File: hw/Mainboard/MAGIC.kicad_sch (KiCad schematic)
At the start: 22 parts, among them SW1 NMI, SW2 RESET, SW4 RESET, U13 Raspberry Pi Zero, U18 SN74LVC4245APWR, U19 SN74LVC4245APWR, U20 SN74LVC4245APWR

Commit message: hw: wip add MCU, 2 layer board
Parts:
- removed C21: 100n, Capacitor_SMD:C_0402_1005Metric, symbol Device:C_Small
- removed SW2: RESET, Button_Switch_THT:SW_Tactile_SPST_Angled_PTS645Vx39-2LFS, symbol Switch:SW_Push
- removed U13: Raspberry Pi Zero, PET:Raspberry Pi Zero W 2, symbol PET:Raspberry Pi Zero W
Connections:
- net A3: now also U19.17 (B5); no longer U19.18 (B4)
- net BA3: now also U19.7 (A5); no longer U19.6 (A4)
- net BHORIZ: now also U20.3 (A1); no longer U20.8 (A6)
- net BR~{W}: now also U20.8 (A6); no longer U19.8 (A6)
- net BVERT: now also U20.4 (A2); no longer U20.9 (A7)
- net B~{PIA1_CS}: now also U20.7 (A5); no longer U20.5 (A3)
- net B~{PIA2_CS}: now also U20.10 (A8); no longer U20.6 (A4)
- net B~{RES}: now also U19.6 (A4); no longer U19.7 (A5)
- net B~{VIA_CS}: now also U20.9 (A7); no longer U20.4 (A2)
- net Bϕ2: now also U20.6 (A4); no longer U20.3 (A1)
- net GND: now also U19.16 (B6); no longer U20.17 (B5)
- net HORIZ: now also U20.21 (B1); no longer U20.16 (B6)
- net R~{W}: now also U20.16 (B6); no longer U19.16 (B6)
- net VERT: now also U20.20 (B2); no longer U20.15 (B7)
- net ~{BVIDEO}: now also U20.5 (A3); no longer U20.10 (A8)
- net ~{PIA1_CS}: now also U20.17 (B5); no longer U20.19 (B3)
- net ~{PIA2_CS}: now also U20.14 (B8); no longer U20.18 (B4)
- net ~{RES}: now also U19.18 (B4); no longer U19.17 (B5)
- net ~{VIA_CS}: now also U20.15 (B7); no longer U20.20 (B2)
- net ~{VIDEO}: now also U20.19 (B3); no longer U20.14 (B8)
- net ϕ2: now also U20.18 (B4); no longer U20.21 (B1)
- no-connect marks 5 -> 3
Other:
- added sheet MCU (MCU.kicad_sch)
- note added: "Shift 5V -> 3.3V: VOUT = VIN * (R2 / (R1 + R2) VIN = 5.1V R1 = 5.6k - 1% R2 = 10k + 1% VOUT = 3.29V"
- note removed: "GPIO2/3 have built-in 1k8 pull ups"
- moved on the sheet: C24, C25, SW1, SW4

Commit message: hw: T8 (wip)
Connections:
- net BHORIZ: now also U20.5 (A3); no longer U20.3 (A1)
- net HORIZ: now also U20.19 (B3); no longer U20.21 (B1)
- net ~{BVIDEO}: now also U20.3 (A1); no longer U20.5 (A3)
- net ~{VIDEO}: now also U20.21 (B1); no longer U20.19 (B3)
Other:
- sheet CPLD ports: added ~{ML}, ~{SO}, ~{VP}; removed A[0..16], D[0..7], PI_A[0..15], PI_CLK, PI_D[0..7], PI_R~{W}, RAM_A[10..11], ~{PI_DONE}, ~{PI_PENDING}
- moved on the sheet: R52, R54, R55, R57, R58, R60

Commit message: hw: routing (excluding MCU)
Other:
- sheet CPLD renamed FPGA
- sheet FPGA ports: added A[0..16], D[0..7], MCU_CLK, RAM_A[10..11], SPI0_RX, SPI0_SCK, SPI0_TX, SPI0_~{CS}, SPI1_RX, SPI1_SCK, SPI1_TX, SPI1_~{CS}, SPI1_~{READY}, ~{CRESET}; removed none
- sheet MCU ports: added MCU_CLK, SPI0_SCK, SPI1_SCK, ~{CRESET}; removed MCU_SPI1_SCLK, SPI0_SCLK
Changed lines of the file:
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@@
+    (stroke (width 0) (type default) (color 0 0 0 0))
+  )
+  (wire (pts (xy 102.87 44.45) (xy 109.22 44.45))
     (stroke (width 0) (type default) (color 0 0 0 0))
   )
@@
     (stroke (width 0) (type default) (color 0 0 0 0))
   )
+  (wire (pts (xy 102.87 68.58) (xy 109.22 68.58))
+    (stroke (width 0) (type default) (color 0 0 0 0))
+  )
   (wire (pts (xy 261.62 144.78) (xy 265.43 144.78))
     (stroke (width 0) (type default) (color 0 0 0 0))
@@
     (stroke (width 0) (type default) (color 0 0 0 0))
   )
+  (wire (pts (xy 102.87 71.12) (xy 109.22 71.12))
+    (stroke (width 0) (type default) (color 0 0 0 0))
+  )
+  (wire (pts (xy 102.87 58.42) (xy 109.22 58.42))
+    (stroke (width 0) (type default) (color 0 0 0 0))
+  )
   (wire (pts (xy 232.41 52.07) (xy 233.68 52.07))
     (stroke (width 0) (type default) (color 0 0 0 0))
@@
     (stroke (width 0) (type default) (color 0 0 0 0))
   )
+  (wire (pts (xy 102.87 39.37) (xy 109.22 39.37))
+    (stroke (width 0) (type default) (color 0 0 0 0))
+  )
   (wire (pts (xy 247.65 76.2) (xy 245.11 76.2))
     (stroke (width 0) (type default) (color 0 0 0 0))
@@
     (stroke (width 0) (type default) (color 0 0 0 0))
   )
+  (wire (pts (xy 102.87 60.96) (xy 109.22 60.96))
+    (stroke (width 0) (type default) (color 0 0 0 0))
+  )
   (wire (pts (xy 262.89 129.54) (xy 261.62 129.54))
     (stroke (width 0) (type default) (color 0 0 0 0))
   )
+  (wire (pts (xy 102.87 55.88) (xy 109.22 55.88))
+    (stroke (width 0) (type default) (color 0 0 0 0))
+  )
   (wire (pts (xy 33.02 139.7) (xy 44.45 139.7))
     (stroke (width 0) (type default) (color 0 0 0 0))
@@
     (stroke (width 0) (type default) (color 0 0 0 0))
   )
+  (wire (pts (xy 102.87 53.34) (xy 109.22 53.34))
+    (stroke (width 0) (type default) (color 0 0 0 0))
+  )
   (wire (pts (xy 149.86 133.35) (xy 149.86 140.97))
     (stroke (width 0) (type default) (color 0 0 0 0))
   )
+  (wire (pts (xy 102.87 41.91) (xy 109.22 41.91))
+    (stroke (width 0) (type default) (color 0 0 0 0))
+  )
   (wire (pts (xy 232.41 46.99) (xy 232.41 49.53))
     (stroke (width 0) (type default) (color 0 0 0 0))
@@
     (stroke (width 0) (type default) (color 0 0 0 0))
   )
+  (wire (pts (xy 102.87 63.5) (xy 109.22 63.5))
+    (stroke (width 0) (type default) (color 0 0 0 0))
+  )
   (wire (pts (xy 204.47 46.99) (xy 208.28 46.99))
     (stroke (width 0) (type default) (color 0 0 0 0))
@@
   )
   (bus (pts (xy 201.93 41.91) (xy 201.93 44.45))
+    (stroke (width 0) (type default) (color 0 0 0 0))
+  )
+  (wire (pts (xy 102.87 46.99) (xy 109.22 46.99))
     (stroke (width 0) (type default) (color 0 0 0 0))
   )
@@
     (stroke (width 0) (type solid) (color 0 0 0 0))
     (fill (color 0 0 0 0.0000))
-    (property "Sheet name" "CPLD" (id 0) (at 109.22 33.5784 0)
+    (property "Sheet name" "FPGA" (id 0) (at 109.22 33.5784 0)
       (effects (font (size 1.27 1.27)) (justify left bottom))
     )
@@
       (effects (font (size 1.27 1.27)) (justify right))
     )
-  )
-  (sheet (at 31.75 27.94) (size 38.1 50.8) (fields_autoplaced)
+    (pin "D[0..7]" bidirectional (at 139.7 44.45 0)
+      (effects (font (size 1.27 1.27)) (justify right))
+    )
+    (pin "RAM_A[10..11]" output (at 139.7 39.37 0)
+      (effects (font (size 1.27 1.27)) (justify right))
+    )
+    (pin "A[0..16]" bidirectional (at 139.7 41.91 0)
+      (effects (font (size 1.27 1.27)) (justify right))
+    )
+    (pin "SPI0_RX" output (at 109.22 44.45 180)
+      (effects (font (size 1.27 1.27)) (justify left))
+    )
+    (pin "SPI0_TX" input (at 109.22 46.99 180)
+      (effects (font (size 1.27 1.27)) (justify left))
+    )
+    (pin "SPI0_~{CS}" input (at 109.22 39.37 180)
+      (effects (font (size 1.27 1.27)) (justify left))
+    )
+    (pin "SPI1_RX" output (at 109.22 58.42 180)
+      (effects (font (size 1.27 1.27)) (justify left))
+    )
+    (pin "SPI1_~{CS}" input (at 109.22 53.34 180)
+      (effects (font (size 1.27 1.27)) (justify left))
+    )
+    (pin "SPI1_TX" input (at 109.22 60.96 180)
+      (effects (font (size 1.27 1.27)) (justify left))
+    )
+    (pin "MCU_CLK" input (at 109.22 68.58 180)
+      (effects (font (size 1.27 1.27)) (justify left))
+    )
+    (pin "SPI0_SCK" input (at 109.22 41.91 180)
+      (effects (font (size 1.27 1.27)) (justify left))
+    )
+    (pin "SPI1_~{READY}" output (at 109.22 63.5 180)
+      (effects (font (size 1.27 1.27)) (justify left))
+    )
+    (pin "SPI1_SCK" input (at 109.22 55.88 180)
+      (effects (font (size 1.27 1.27)) (justify left))
+    )
+    (pin "~{CRESET}" input (at 109.22 71.12 180)
+      (effects (font (size 1.27 1.27)) (justify left))
+    )
+  )
+  (sheet (at 64.77 34.29) (size 38.1 50.8) (fields_autoplaced)
     (stroke (width 0.1524) (type solid) (color 0 0 0 0))
     (fill (color 0 0 0 0.0000))
-    (property "Sheet name" "MCU" (id 0) (at 31.75 27.2284 0)
+    (property "Sheet name" "MCU" (id 0) (at 64.77 33.5784 0)
       (effects (font (size 1.27 1.27)) (justify left bottom))
     )
-    (property "Sheet file" "MCU.kicad_sch" (id 1) (at 31.75 79.3246 0)
+    (property "Sheet file" "MCU.kicad_sch" (id 1) (at 64.77 85.6746 0)
       (effects (font (size 1.27 1.27)) (justify left top))
     )
-    (pin "SPI0_SCLK" output (at 69.85 35.56 0)
-      (effects (font (size 1.27 1.27)) (justify right))
-    )
-    (pin "SPI0_~{CS}" output (at 69.85 33.02 0)
-      (effects (font (size 1.27 1.27)) (justify right))
-    )
-    (pin "SPI0_RX" input (at 69.85 38.1 0)
-      (effects (font (size 1.27 1.27)) (justify right))
-    )
-    (pin "SPI0_TX" output (at 69.85 40.64 0)
-      (effects (font (size 1.27 1.27)) (justify right))
-    )
-    (pin "MCU_SPI1_SCLK" output (at 69.85 48.26 0)
-      (effects (font (size 1.27 1.27)) (justify right))
-    )
-    (pin "SPI1_~{CS}" output (at 69.85 45.72 0)
-      (effects (font (size 1.27 1.27)) (justify right))
-    )
-    (pin "SPI1_RX" input (at 69.85 50.8 0)
-      (effects (font (size 1.27 1.27)) (justify right))
-    )
-    (pin "SPI1_TX" output (at 69.85 53.34 0)
-      (effects (font (size 1.27 1.27)) (justify right))
-    )
-    (pin "SPI1_~{READY}" input (at 69.85 55.88 0)
-      (effects (font (size 1.27 1.27)) (justify right))
-    )
+    (pin "SPI0_~{CS}" output (at 102.87 39.37 0)
+      (effects (font (size 1.27 1.27)) (justify right))
+    )
+    (pin "SPI0_RX" input (at 102.87 44.45 0)
+      (effects (font (size 1.27 1.27)) (justify right))
+    )
+    (pin "SPI0_TX" output (at 102.87 46.99 0)
+      (effects (font (size 1.27 1.27)) (justify right))
+    )
+    (pin "SPI1_~{CS}" output (at 102.87 53.34 0)
+      (effects (font (size 1.27 1.27)) (justify right))
+    )
+    (pin "SPI1_RX" input (at 102.87 58.42 0)
+      (effects (font (size 1.27 1.27)) (justify right))
+    )
+    (pin "SPI1_TX" output (at 102.87 60.96 0)
+      (effects (font (size 1.27 1.27)) (justify right))
+    )
+    (pin "SPI1_~{READY}" input (at 102.87 63.5 0)
+      (effects (font (size 1.27 1.27)) (justify right))
+    )
+    (pin "SPI1_SCK" output (at 102.87 55.88 0)
+      (effects (font (size 1.27 1.27)) (justify right))
+    )
+    (pin "MCU_CLK" output (at 102.87 68.58 0)
+      (effects (font (size 1.27 1.27)) (justify right))
+    )
+    (pin "SPI0_SCK" output (at 102.87 41.91 0)
+      (effects (font (size 1.27 1.27)) (justify right))
+    )
+    (pin "~{CRESET}" output (at 102.87 71.12 0)
+      (effects (font (size 1.27 1.27)) (justify right))
+    )

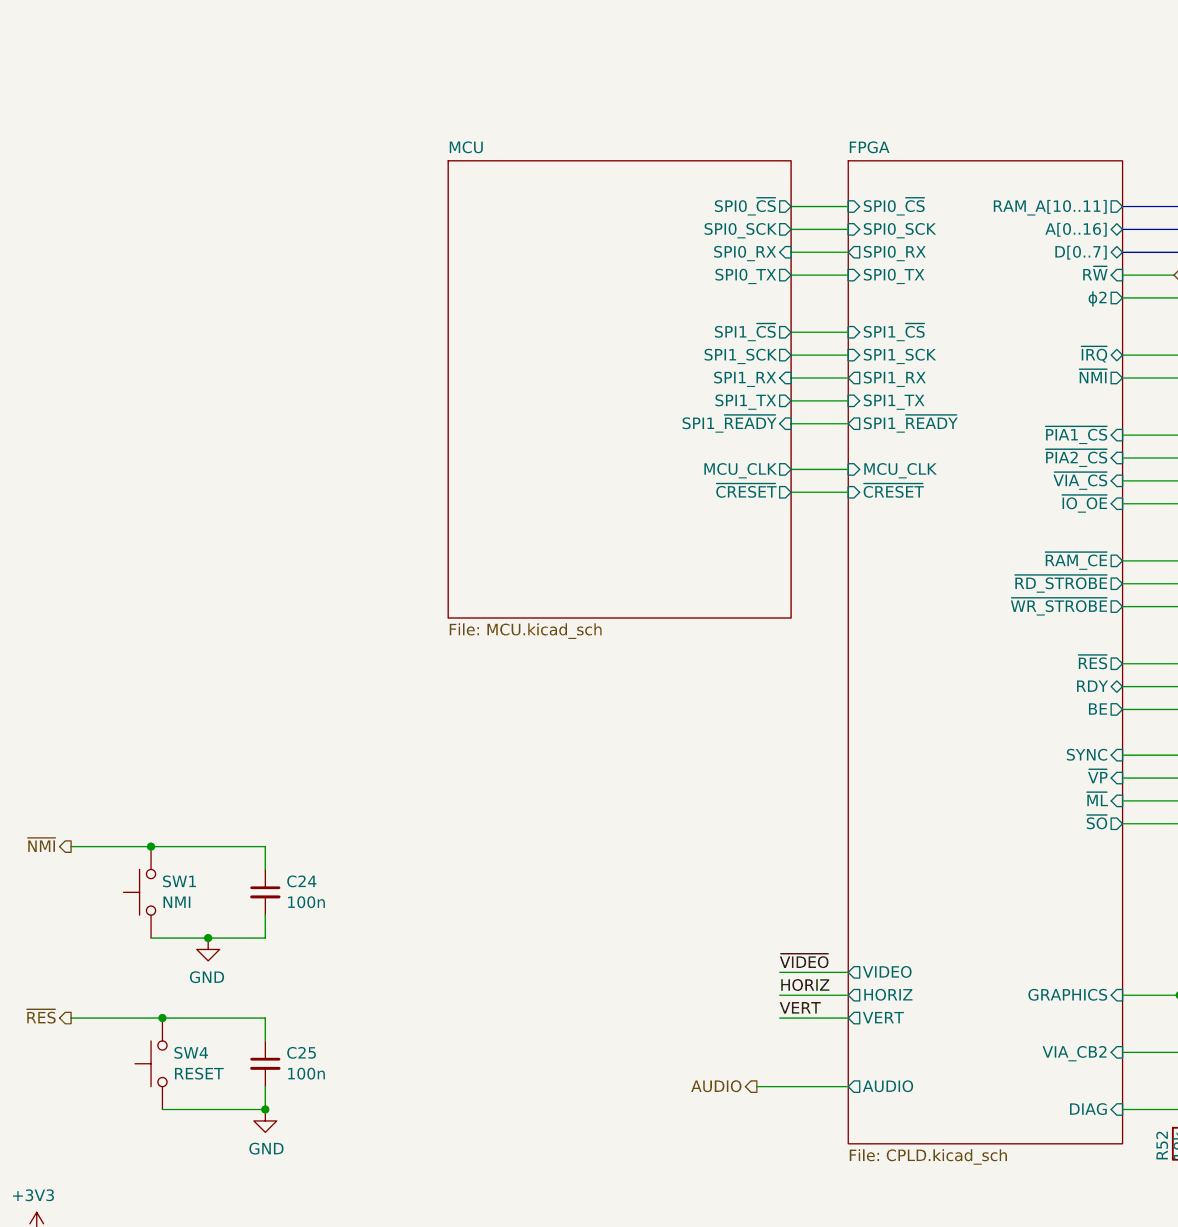
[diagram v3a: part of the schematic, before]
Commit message: hw: routed, but trace sizes need to be reviewed/fixed
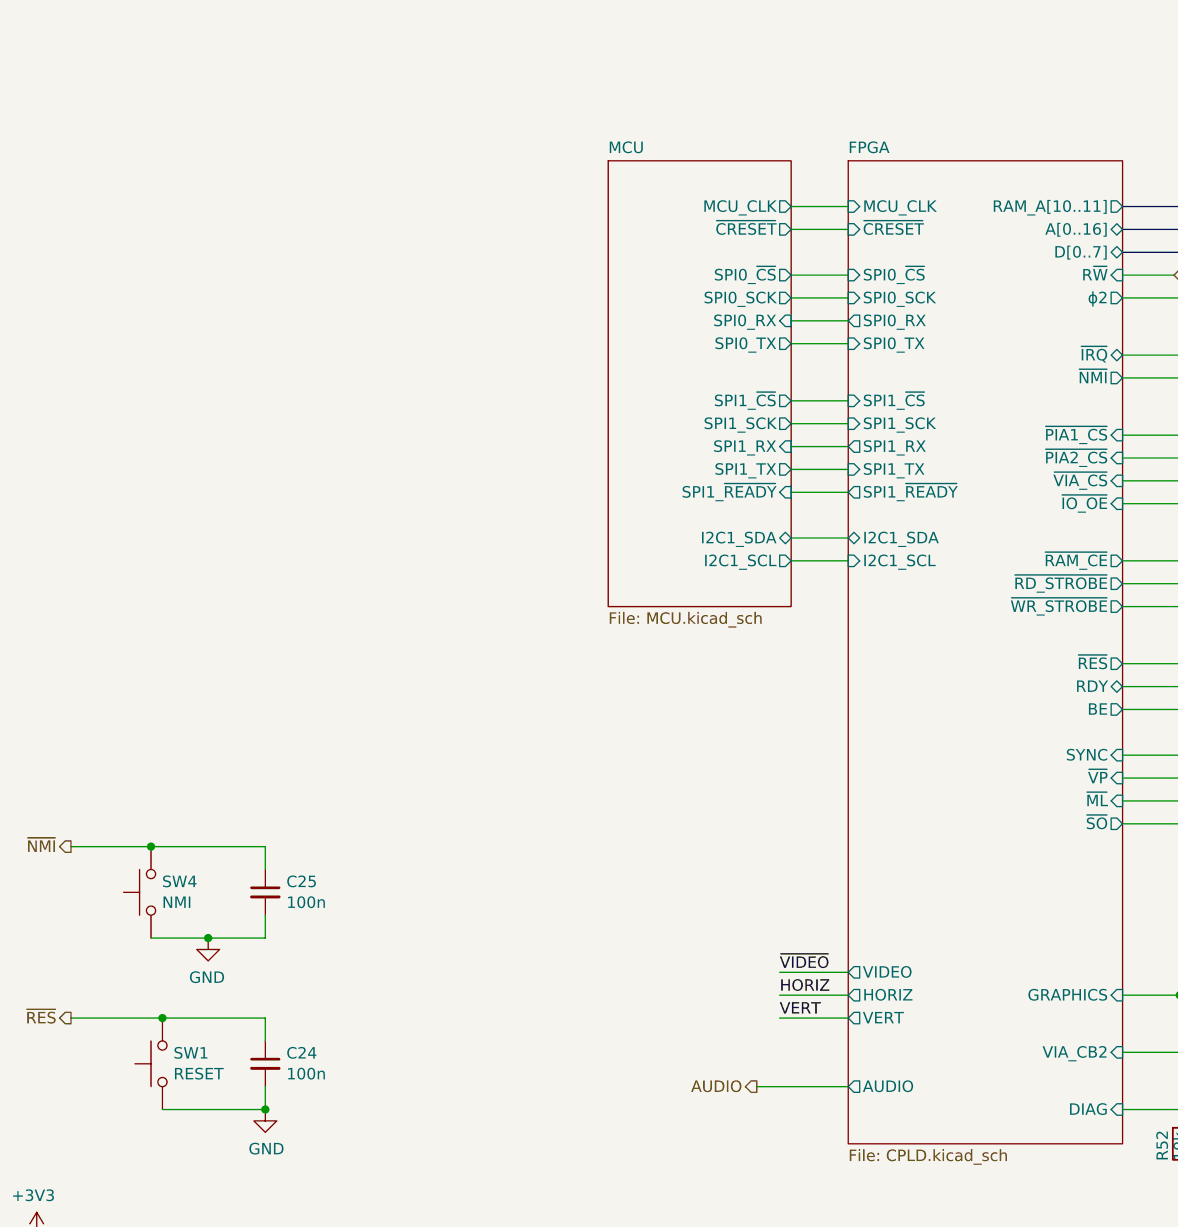
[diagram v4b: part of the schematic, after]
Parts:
- renumbered C25 to C24, C24 to C25, SW4 to SW1, SW1 to SW4
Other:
- sheet FPGA ports: added I2C1_SCL, I2C1_SDA; removed none
- sheet MCU ports: added I2C1_SCL, I2C1_SDA; removed none

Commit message: hw: wip
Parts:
- SW1, SW4: footprint Button_Switch_THT:SW_PUSH_6mm -> JLCPCB:SW-TH_L6.0-W3.5-P6.50
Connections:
- net GND: no longer C24.2, C25.2, SW1.1, SW4.1
- new net PD_GND: C24.2, C25.2, SW1.1, SW4.1
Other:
- sheet FPGA ports: added ~{FPGA_PROG}; removed none
- sheet MCU ports: added ~{FPGA_PROG}; removed none
- moved on the sheet: C24, C25, SW1, SW4
